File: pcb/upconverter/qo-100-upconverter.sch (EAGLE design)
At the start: 172 parts, among them CON1 3P-SH-SIDE, CON2 2EDG-2P-5MM, U1 EFM32TG11B120F128GM32, U10 MIC23155, U11 LT8636, U12 MCP3421-A0, U13 MCP6C02-020, U14 ADP7142AUJZ-3.3, U15 ADP7142AUJZ-3.3, U16 ADP3334, U17 ADM7171ACPZ-5.0, U2 DSB321SDA, U3 ADF4351, U4 F1951NBGI, U5 MAX2671, U6 2450BP15E0100, U7 F1478NLGA, U8 F1951NBGI, U9 ADL5606

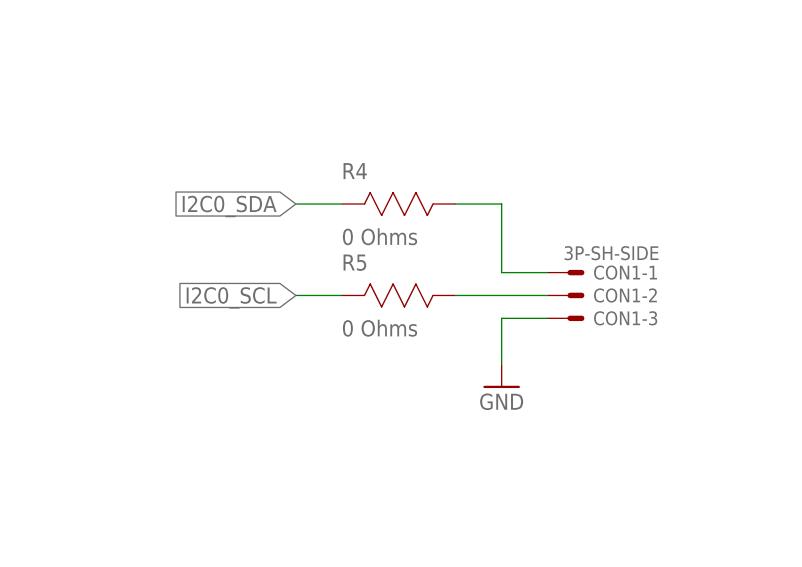
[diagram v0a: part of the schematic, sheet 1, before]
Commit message: Upconverter assembly BOM changes
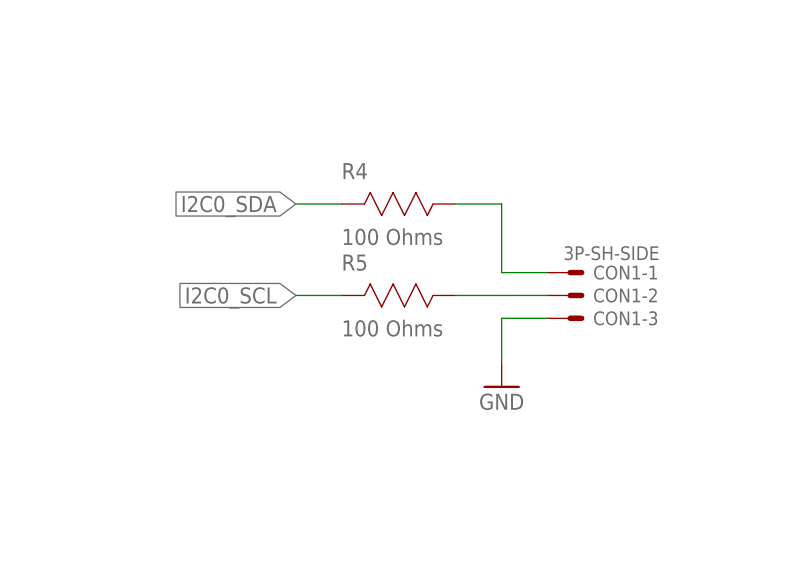
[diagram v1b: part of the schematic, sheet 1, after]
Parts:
- C25: value 100nF -> 150pF
- C27: value 100nF -> 150pF + 18 nH
- R4, R5: value 0 Ohms -> 100 Ohms
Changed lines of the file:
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@@
 <part name="U5" library="Maxim Integrated" deviceset="MAX2671" device=""/>
 <part name="RFCON1" library="RF Connector" deviceset="RFCON" device="-SMA-EDGE"/>
-<part name="C25" library="Capacitor" deviceset="CAPACITOR" device="-0603" value="100nF"/>
+<part name="C25" library="Capacitor" deviceset="CAPACITOR" device="-0603" value="150pF"/>
 <part name="GND2" library="Supply Symbol" deviceset="GND" device=""/>
 <part name="GND3" library="Supply Symbol" deviceset="GND" device=""/>
@@
 <part name="GND73" library="Supply Symbol" deviceset="GND" device=""/>
 <part name="U4" library="Renesas" deviceset="F1951*" device="" technology="NBGI"/>
-<part name="C27" library="Capacitor" deviceset="CAPACITOR" device="-0603" value="100nF"/>
+<part name="C27" library="Capacitor" deviceset="CAPACITOR" device="-0603" value="150pF + 18 nH"/>
 <part name="R14" library="Resistor" deviceset="RESISTOR" device="-0603" value="61.9 Ohms"/>
 <part name="R12" library="Resistor" deviceset="RESISTOR" device="-0603" value="105 Ohms"/>
@@
 <part name="CON1" library="JST" deviceset="3P" device="-SH-SIDE" value="3P-SH-SIDE"/>
 <part name="GND43" library="Supply Symbol" deviceset="GND" device=""/>
-<part name="R4" library="Resistor" deviceset="RESISTOR" device="-0603" value="0 Ohms"/>
-<part name="R5" library="Resistor" deviceset="RESISTOR" device="-0603" value="0 Ohms"/>
+<part name="R4" library="Resistor" deviceset="RESISTOR" device="-0603" value="100 Ohms"/>
+<part name="R5" library="Resistor" deviceset="RESISTOR" device="-0603" value="100 Ohms"/>
 <part name="U13" library="Microchip" deviceset="MCP6C02" device="" technology="-020"/>
 <part name="R36" library="Resistor" deviceset="RESISTOR" device="-1206" value="0.03 Ohms">

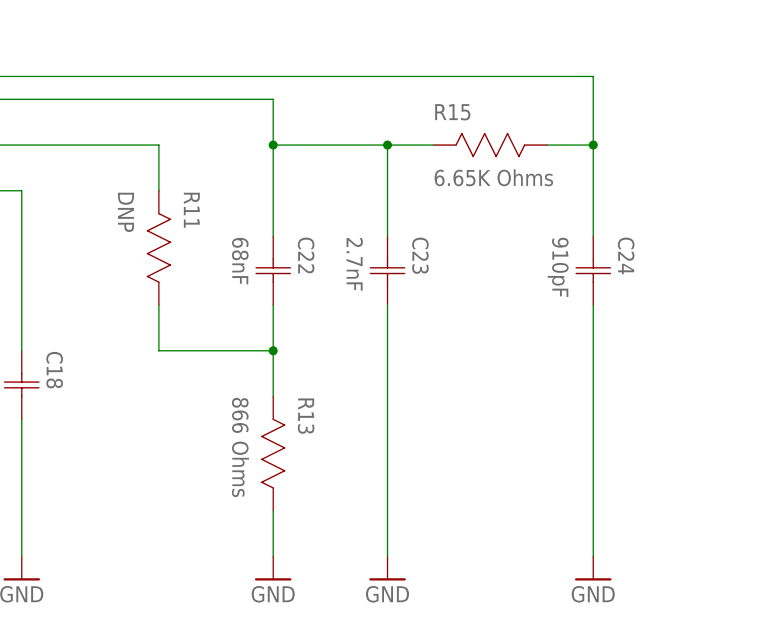
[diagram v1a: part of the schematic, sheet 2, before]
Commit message: Tweaking upconverter performance
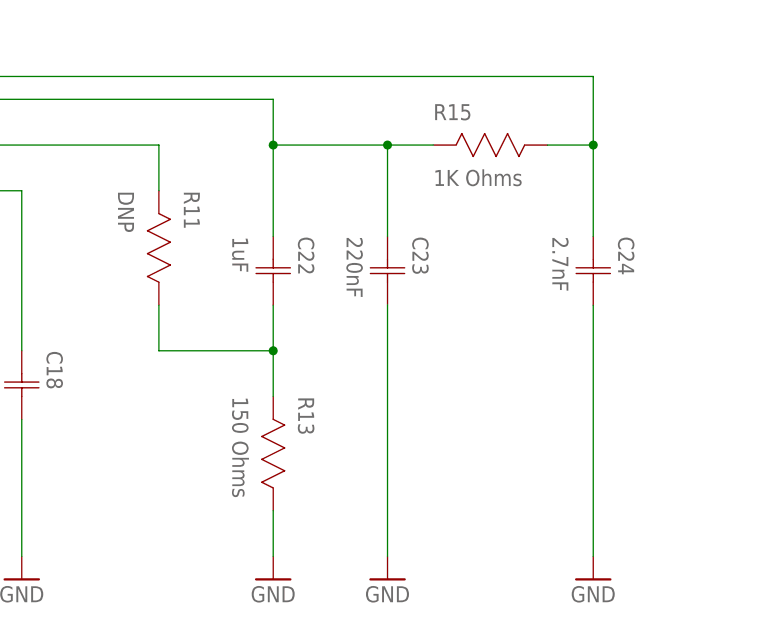
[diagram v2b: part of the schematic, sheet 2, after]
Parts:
- C22: value 68nF -> 1uF
- C23: value 2.7nF -> 220nF
- C24: value 910pF -> 2.7nF
- R13: value 866 Ohms -> 150 Ohms
- R15: value 6.65K Ohms -> 1K Ohms
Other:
- note added: "2kHz Loop Bandwidth at 2 mA"
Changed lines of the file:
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@@
 <part name="C10" library="Capacitor" deviceset="CAPACITOR" device="-0603" value="100nF"/>
 <part name="GND607" library="Supply Symbol" deviceset="GND" device=""/>
-<part name="C23" library="Capacitor" deviceset="CAPACITOR" device="-0603" value="2.7nF"/>
-<part name="C22" library="Capacitor" deviceset="CAPACITOR" device="-0603" value="68nF"/>
-<part name="R13" library="Resistor" deviceset="RESISTOR" device="-0603" value="866 Ohms"/>
-<part name="C24" library="Capacitor" deviceset="CAPACITOR" device="-0603" value="910pF"/>
-<part name="R15" library="Resistor" deviceset="RESISTOR" device="-0603" value="6.65K Ohms"/>
+<part name="C23" library="Capacitor" deviceset="CAPACITOR" device="-0603" value="220nF"/>
+<part name="C22" library="Capacitor" deviceset="CAPACITOR" device="-0603" value="1uF"/>
+<part name="R13" library="Resistor" deviceset="RESISTOR" device="-0603" value="150 Ohms"/>
+<part name="C24" library="Capacitor" deviceset="CAPACITOR" device="-0603" value="2.7nF"/>
+<part name="R15" library="Resistor" deviceset="RESISTOR" device="-0603" value="1K Ohms"/>
 <part name="GND618" library="Supply Symbol" deviceset="GND" device=""/>
 <part name="GND620" library="Supply Symbol" deviceset="GND" device=""/>
@@
 <plain>
 <text x="441.96" y="248.92" size="1.778" layer="98" align="center">-9 dB Pi Attenuator</text>
+<text x="444.5" y="170.18" size="1.778" layer="98" align="center">2kHz Loop Bandwidth at 2 mA</text>
 </plain>
 <instances>

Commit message: Upconverter v3 sent to production
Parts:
- added C100, C101, C99: 10uF, Capacitor:CAPACITOR-0603
- added C102, C103: 1nF, Capacitor:CAPACITOR-0603
- added C104: 10uF, Capacitor:CAPACITOR-1206
- added C87, C91, C92: 100nF, Capacitor:CAPACITOR-0603
- added C88: 10pF, Capacitor:CAPACITOR-0603
- added C89, C94, C95, C96, C97, C98: 1uF, Capacitor:CAPACITOR-0603
- added C90: 100uF, Capacitor:CAPACITOR-1206
- added C93: 22uF, Capacitor:CAPACITOR-1206
- added L12, L13: 3.3nH, Inductor:INDUCTOR-0603
- added L14: 1.8nH, Inductor:INDUCTOR-0603
- added L15: 1.5nH, Inductor:INDUCTOR-0603
- added L16: 470nH, Inductor:INDUCTOR-0603
- added L17: 2.2nH, Inductor:INDUCTOR-0603
- added L18: 62nH, Inductor:INDUCTOR-0603
- added L19: 0 Ohms, Inductor:INDUCTOR-0603
- added L20: 4.7uH, Inductor:INDUCTOR-6X6MM
- added R44: 75K Ohms, Resistor:RESISTOR-0603
- added R45: 41.2K Ohms, Resistor:RESISTOR-0603
- added R46: 1M Ohms, Resistor:RESISTOR-0603
- added R47: 221K Ohms, Resistor:RESISTOR-0603
- added R48, R49: 10K Ohms, Resistor:RESISTOR-0603
- added R50: 0.03 Ohms, Resistor:RESISTOR-1206
- added R51, R52: 100K Ohms, Resistor:RESISTOR-0603
- added R53: 1K Ohms, Resistor:RESISTOR-0603
- added RFCON5, RFCON6, RFCON7: RFCON-U.FL, RF Connector:RFCON-U.FL
- added RFCON8: RFCON-SMA-EDGE, RF Connector:RFCON-SMA-EDGE
- added SHIELD1: SHIELD-TE-2118728, Shield:SHIELD-TE-2118728
- added TP1, TP2, TP3, TP4, TP5, TP6: TESTPOINT-1.27MM, PADs:TESTPOINT-1.27MM
- added U18: MCP3421-A0, Microchip:MCP3421-A0
- added U19: MCP6C02-020, Microchip:MCP6C02-020
- added U20, U21, U22: ADP7142AUJZ-3.3, Analog Devices:ADP7142AUJZ-3.3
- added U23, U24: ADM7171ACPZ-5.0, Analog Devices:ADM7171ACPZ-5.0
- C10: value 100nF -> 10pF
- C25: value 150pF -> 1uF
- C26: value 100nF -> 1.2pF
- C27: value 150pF + 18 nH -> 100nF
- C28, C4: value 1uF -> 100nF
- C29: value 100nF -> 150pF
- C30: value 100pF -> 47pF
- C31: value 47pF -> 1.8pF
- C32: value 47pF -> 1.5pF
- C33: value 220pF -> 1.5pF
- C34: value 100uF -> 150pF; device Capacitor:CAPACITOR-1206 -> Capacitor:CAPACITOR-0603
- C35: value 1uF -> 220pF
- C36: value 1nF -> 100uF; device Capacitor:CAPACITOR-0603 -> Capacitor:CAPACITOR-1206
- C37: value 0.5pF -> 1uF
- C38, C55, C7: value 15pF -> 100nF
- C39: value 10pF -> 1uF
- C40: value 1uF -> 33pF
- C41: value 1nF -> 100nF
- C42: value 15pF -> 0.8pF
- C43, C9: value 10pF -> 100nF
- C44: value 1.2pF -> 10pF
- C45: value 100nF -> 47pF
- C46: value 15pF -> 1uF
- C47: value 10uF -> 15pF
- C48: value 10nF -> 100nF
- C49: value 100uF -> 33pF; device Capacitor:CAPACITOR-1206 -> Capacitor:CAPACITOR-0603
- C5: value 100nF -> 1uF
- C50: value 100pF -> 15pF
- C51: value 2pF -> 15pF
- C52: value 1uF -> 22pF
- C53: value 10nF -> 0.7pF
- C54: value 100pF -> 4.7uF
- C56: value 3.3pF -> 15pF
- C57: value 15pF -> 10nF
- C58: value 4.7uF -> 1uF; VOLTAGE 35V -> (none)
- C59: value 100nF -> 10uF
- C60: value 470pF -> 10nF
- C61: value 470pF -> 15pF
- C62: value 4.7uF -> 10nF
- C63: value 1uF -> 100uF; device Capacitor:CAPACITOR-0603 -> Capacitor:CAPACITOR-1206; VOLTAGE 50V -> (none)
- C64: value 470pF -> 100pF
- C65: value 1uF -> 2pF; VOLTAGE 50V -> (none)
- C68: value 100nF -> 100pF
- C69: value 100nF -> 15pF
- C70: value 10pF -> 3.3pF
- C71: value 1uF -> 15pF
- C73: value 100uF -> 15pF; device Capacitor:CAPACITOR-1206 -> Capacitor:CAPACITOR-0603
- C74: value 100uF -> 4.7uF; device Capacitor:CAPACITOR-1206 -> Capacitor:CAPACITOR-0603; VOLTAGE (none) -> 35V
- C76: value 100nF -> 470pF
- C77: value 22uF -> 470pF; device Capacitor:CAPACITOR-1206 -> Capacitor:CAPACITOR-0603
- C78: value 1uF -> 4.7uF
- C79, C80: VOLTAGE (none) -> 50V
- C82: value 10uF -> 10nF
- C83: value 10uF -> 100nF
- C84: value 1nF -> 10uF
- C85: value 470pF -> 10uF
- C86: value 10uF -> 100nF; device Capacitor:CAPACITOR-1206 -> Capacitor:CAPACITOR-0603; VOLTAGE 50V -> (none)
- L1: value 3.3nH -> 1uH
- L10: value 2.2uH -> 3.9nH; device Inductor:INDUCTOR-2.5X2X1.2MM -> Inductor:INDUCTOR-0603; CURRENT 2.2A -> (none); OCLCSC C375952 -> (none)
- L11: value 4.7uH -> 5.6nH; device Inductor:INDUCTOR-6X6MM -> Inductor:INDUCTOR-0603; CURRENT 3A -> (none); OCLCSC C326336 -> (none)
- L2: value 10nH -> 3.3nH
- L3: value 3.3nH -> 10nH
- L5: value 1.8nH -> 4.7nH
- L6: value 3.9nH -> 12nH
- L7: value 3nH -> 3.3nH
- L8: value 62nH -> 3.9nH
- L9: value 62nH -> 18nH
- R10: value 5.1K Ohms -> 100K Ohms
- R11: value DNP -> 330 Ohms
- R12: value 105 Ohms -> 0 Ohms
- R13: value 150 Ohms -> 10K Ohms
- R14: value 61.9 Ohms -> 5.1K Ohms
- R15, R23: value 1K Ohms -> DNP
- R17: value 1K Ohms -> 150 Ohms
- R18: value 100 Ohms -> 61.9 Ohms
- R19: value 100K Ohms -> 1K Ohms
- R20: value 0 Ohms -> 105 Ohms; device Resistor:RESISTOR-SEL-0603 -> Resistor:RESISTOR-0603
- R22, R24: value 510 Ohms -> 0 Ohms
- R25: value 100K Ohms -> DNP
- R26, R35: value 10K Ohms -> DNP
- R27: value 100K Ohms -> 0 Ohms
- R28: value 75K Ohms -> 1K Ohms
- R29: value 41.2K Ohms -> 0 Ohms
- R30: value 309K Ohms -> DNP
- R31: value 71.5K Ohms -> 1.5K Ohms
- R32: value 1M Ohms -> 0 Ohms
- R33: value 221K Ohms -> 510 Ohms
- R34: value 10K Ohms -> 0 Ohms
- R36: value 0.03 Ohms -> 1K Ohms; device Resistor:RESISTOR-1206 -> Resistor:RESISTOR-0603; TOLERANCE 1% -> (none)
- R37: value 100K Ohms -> 2K Ohms
- R38, R7: value 100K Ohms -> 100 Ohms
- R39: value 210K Ohms -> 49.9 Ohms
- R4, R5: value 100 Ohms -> 1K Ohms
- R40: value 64.9K Ohms -> 510 Ohms
- R41: value 510 Ohms -> 100K Ohms
- R43: value 0 Ohms -> 100K Ohms
- R6: value 330 Ohms -> 100 Ohms
- R8: value 100K Ohms -> 330 Ohms
- R9: value 330 Ohms -> 100K Ohms
- RFCON1, RFCON3: value RFCON-SMA-EDGE -> RFCON-U.FL; device RF Connector:RFCON-SMA-EDGE -> RF Connector:RFCON-U.FL
- RFCON2: value RFCON-U.FL -> RFCON-SMA-EDGE; device RF Connector:RFCON-U.FL -> RF Connector:RFCON-SMA-EDGE
- U10: value MIC23155 -> LTC5597; device Microchip:MIC23155 -> Analog Devices:LTC5597
- U11: value LT8636 -> 2450BP15E0100; device Analog Devices:LT8636 -> Generic Filter:2450BP15E0100
- U12: value MCP3421-A0 -> MCP6V31; device Microchip:MCP3421-A0 -> Microchip:MCP6V31
- U13: value MCP6C02-020 -> DC2337J5010AHF; device Microchip:MCP6C02-020 -> Anaren:DC2337J5010AHF; OCLCSC (none) -> C509396
- U14: value ADP7142AUJZ-3.3 -> ADL5606; device Analog Devices:ADP7142AUJZ-3.3 -> Analog Devices:ADL5606
- U15: value ADP7142AUJZ-3.3 -> F1958NBGK; device Analog Devices:ADP7142AUJZ-3.3 -> Renesas:F1958NBGK
- U16: value ADP3334 -> MCP1700-330; device Analog Devices:ADP3334 -> Microchip:MCP1700-330
- U17: value ADM7171ACPZ-5.0 -> LT8636; device Analog Devices:ADM7171ACPZ-5.0 -> Analog Devices:LT8636
- U4: value F1951NBGI -> F1958NBGK; device Renesas:F1951NBGI -> Renesas:F1958NBGK
- U7: value F1478NLGA -> F1958NBGK; device Renesas:F1478NLGA -> Renesas:F1958NBGK
- U8: value F1951NBGI -> ADL5601; device Renesas:F1951NBGI -> Analog Devices:ADL5601
- U9: value ADL5606 -> F1490NLGA; device Analog Devices:ADL5606 -> Renesas:F1490NLGA
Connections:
- removed net !IF_ATT_CS: U1.PC13, U4.!CS
- removed net !PA_STG1_BIAS_EN: R38.1, U1.PA2, U16.SD
- removed net !RF_ATT_CS: U1.PA1, U8.!CS
- removed net 3V3_ATT_MIXER_CLEAN: C26.C1, C28.C1, C29.C1, C31.C1, C32.C1, C45.C1, C7.C1, C82.C1, L5.2, U14.SENSE/ADJ, U14.VOUT, U4.VDD, U5.VCC, U8.VDD
- removed net 3V3_FB: R30.1, R31.2, U10.FB
- removed net 3V3_SOFTSTART: C64.C1, U10.SS
- removed net 3V3_SW: L10.1, U10.SW
- removed net 5V0_PA_STG1_CLEAN: C34.C1, C35.C1, C36.C1, C38.C1, C40.C1, C41.C1, C42.C1, C85.C1, L7.2, L8.2, R22.2, R39.2, U16.OUT, U7.BIAS1
- removed net 5V0_PA_STG2_CLEAN: C47.C1, C48.C1, C49.C1, C50.C1, C52.C1, C53.C1, C54.C1, C55.C1, L9.2, R24.2, U17.SENSE, U17.VOUT, U9.VBIAS, U9.VCC
- removed net N$14: C43.C1, L8.1, U7.RFOUT
- removed net N$18: C57.C2, RFCON3.SIGNAL
- removed net N$26: C25.C2, U4.RF2
- removed net N$27: C27.C2, U5.IFIN
- removed net N$31: C33.C2, R20.2
- removed net N$9: C46.C1, U8.RF1
- removed net PA_STG2_BIAS_EN: R37.2, U1.PC0, U17.EN
- removed net RF_ACC_FILT: C37.C1, C39.C1, U6.RFOUT
- removed net RF_ACC_PRE: C43.C2, C44.C1, U8.RF2
- new net 3V3_IF_ATT_MIXER_CLEAN: C25.C1, C27.C1, C28.C1, C30.C1, C99.C1, L14.2, U20.SENSE/ADJ, U20.VOUT, U4.VDD, U4.VMODE, U5.VCC
- new net 3V3_RF_ATT_PDET_CLEAN: C100.C1, C41.C1, C54.C1, C55.C1, C72.C1, U10.EN, U10.VCC, U12.PWR.V+, U15.VDD, U15.VMODE, U21.SENSE/ADJ, U21.VOUT, U7.VDD, U7.VMODE
- new net 5V0_PA_STG1_2_CLEAN: C36.C1, C37.C1, C38.C1, C39.C1, C40.C1, C43.C1, C45.C1, C46.C1, C47.C1, C48.C1, C49.C1, L15.2, L16.2, L17.2, R28.2, R29.2, R31.2, R33.2, U23.SENSE, U23.VOUT
- new net 5V0_PA_STG3_CLEAN: C59.C1, C60.C1, C63.C1, C64.C1, C66.C1, C67.C1, C68.C1, C69.C1, L18.2, R40.2, U14.VBIAS, U14.VCC, U24.SENSE, U24.VOUT
- new net IF_ATT_ACC: L9.1, R24.1
- new net IF_ATT_ACC_PROBE: C34.C2, R23.1, R24.2
- new net IF_ATT_DCC: C34.C1, U4.RF1
- new net IF_ATT_LE: U1.PD6, U4.LE
- new net IF_IN_ACC: C29.C2, U4.RF2
- new net MIXER_IN_DCC: L9.2, U5.IFIN
- new net MIXER_OUT_ACC_PROBE: C35.C2, R26.1, R27.2
- new net MIXER_OUT_DCC: L13.1, U5.RFOUT
- new net N$24: R23.2, RFCON3.SIGNAL
- new net N$33: C31.C2, C32.C1, L10.2, L11.1, L8.2
- new net N$34: C32.C2, C33.C1, L11.2, L12.2
- new net N$35: R30.2, RFCON6.SIGNAL
- new net N$39: L19.2, U15.RF2
- new net N$42: R39.2, U13.ISOLATED
- new net N$43: C56.C1, U10.RFIN
- new net N$44: C57.C2, U10.FLTR
- new net N$45: R22.2, U5.LO
- new net N$47: R25.1, RFCON4.SIGNAL
- new net N$48: R35.2, RFCON7.SIGNAL
- new net PA_STG1_2_BIAS_EN: R51.2, U1.PB7, U23.EN
- new net PA_STG3_BIAS_EN: R52.2, U1.PB8, U24.EN
- new net RF_ATT1_LE: U1.PA1, U7.LE
- new net RF_ATT2_LE: U1.PA2, U15.LE
- new net RF_FINAL_ACC: C71.C2, RFCON8.SIGNAL
- new net RF_FINAL_DCC: C70.C1, C71.C1, L18.1, U14.RFOUT
- new net RF_LOL_FLT_ACC: C33.C2, U8.RFIN
- new net RF_PRE1_ACC: C51.C2, U7.RF2
- new net RF_PRE1_ATT_ACC: R32.1, U6.RFIN
- new net RF_PRE1_ATT_ACC_PROBE: C50.C2, R30.1, R32.2
- new net RF_PRE1_ATT_DCC: C50.C1, U7.RF1
- new net RF_PRE1_ATT_FLT_ACC: C42.C1, C44.C1, U6.RFOUT
- new net RF_PRE1_DCC: C51.C1, L16.1, U8.RFOUT
- new net RF_PRE2_ACC: C52.C2, C53.C1, L19.1
- new net RF_PRE2_ATT_ACC: C73.C2, U11.RFIN
- new net RF_PRE2_ATT_DCC: C73.C1, U15.RF1
- new net RF_PRE2_ATT_FLT_ACC: U11.RFOUT, U13.IN
- new net RF_PRE2_ATT_FLT_CPL_ACC: C56.C2, R35.1, U13.COUPLED
- new net RF_PRE2_ATT_FLT_THRU_ACC: C61.C1, U13.OUT
- new net RF_PRE2_DCC: C52.C1, L17.1, U9.RFOUT
- new net VPDET_AMP: R37.1, R38.2, U12.1.OUT
- new net VPDET_FLT: C58.C1, R34.1, U12.1.+IN
- new net VPDET_RAW: C57.C1, R34.2, U10.OUT
- new net VPDET_SENSE: C62.C1, R38.1, U1.PA0
- net !MIXER_SHDN: now also R21.2, U1.PD7, U5.!SHDN; no longer R18.2, U1.PC14
- net !PLL_MUTE: now also R10.2; no longer R8.2
- net 3V3: now also C4.C1, C83.C1, C84.C1, C85.C1, C86.C1, R4.2, R5.2, U16.VOUT, U18.VDD; no longer C11.C1, C68.C1, C72.C1, C73.C1, L10.2, R17.2, R23.2, R30.2, R38.2, U10.SNS, U12.VDD, U3.DVDD
- net 3V3_PLL_CLEAN: now also C101.C1, C7.C1, C9.C1, L1.2, L2.1, L3.2, U22.SENSE/ADJ, U22.VOUT; no longer C10.C1, C5.C1, C83.C1, L1.1, L2.2, U15.SENSE/ADJ, U15.VOUT
- net 5V0: now also C75.C1, C78.C1, C88.C1, C89.C1, C90.C1, C92.C1, L20.2, R43.2, R46.2, R50.2, R53.2, U16.VIN, U17.BIAS, U19.VDD, U19.VIP; no longer C59.C1, C62.C1, C70.C1, C71.C1, C74.C1, C76.C1, L11.2, R27.2, R32.2, R36.2, R41.2, U10.EN, U10.VIN@0, U10.VIN@1, U11.BIAS, U13.VDD, U13.VIP
- net 5V0_BST: now also C87.C2, U17.BST; no longer C69.C2, U11.BST
- net 5V0_FB: now also C88.C2, R46.1, R47.2, U17.FB; no longer C70.C2, R32.1, R33.2, U11.FB
- net 5V0_INTVCC: now also C81.C1, U17.INTVCC, U17.SYNC/MODE; no longer C66.C1, U11.INTVCC, U11.SYNC/MODE
- net 5V0_ISENSE: now also C93.C1, C94.C1, C95.C1, C96.C1, C97.C1, C98.C1, R50.1, U19.VIM, U20.EN, U20.VIN, U21.EN, U21.VIN, U22.EN, U22.VIN, U23.VIN, U24.VIN; no longer C77.C1, C78.C1, C79.C1, C80.C1, C81.C1, R36.1, U13.VIM, U14.EN, U14.VIN, U15.EN, U15.VIN, U16.IN, U17.VIN
- net 5V0_ISENSE_VN: now also C91.C2, R49.1, U18.VIN-; no longer C75.C2, R35.1, U12.VIN-
- net 5V0_ISENSE_VP: now also C91.C1, R48.1, U18.VIN+; no longer C75.C1, R34.1, U12.VIN+
- net 5V0_RT: now also R45.2, U17.RT; no longer R29.2, U11.RT
- net 5V0_SS: now also C82.C1, U17.TR/SS; no longer C67.C1, U11.TR/SS
- net 5V0_SW: now also C87.C1, L20.1, U17.SW; no longer C69.C1, L11.1, U11.SW
- net 5V0_VSENSE: now also C77.C1, R43.1, R44.2; no longer C61.C1, R27.1, R28.2
- net GND: now also C100.C2, C101.C2, C102.C2, C103.C2, C104.C2, C25.C2, C27.C2, C39.C2, C43.C2, C46.C2, C69.C2, C70.C2, C75.C2, C85.C2, C89.C2, C90.C2, C92.C2, C93.C2, C94.C2, C95.C2, C96.C2, C97.C2, C98.C2, C99.C2, L10.1, L12.1, L5.1, L7.1, R14.1, R17.1, R20.1, R36.1, R39.1, R44.1, R45.1, R47.1, R49.2, R51.1, R52.1, R9.1, RFCON5.GND, RFCON6.GND, RFCON7.GND, RFCON8.GND, SHIELD1.GND, TP1.TP, TP2.TP, TP3.TP, TP4.TP, TP5.TP, TP6.TP, U10.GND@0, U10.GND@1, U10.GND@2, U10.GND@3, U12.PWR.V-, U13.GND, U14.DISABLE, U15.D0, U15.D1, U15.D2, U15.D3, U15.D4, U15.D5, U15.D6, U18.VSS, U19.VREF, U19.VSS, U20.GND, U21.GND, U22.GND, U23.GND, U24.GND, U4.D0, U4.D1, U4.D2, U4.D3, U4.D4, U4.D5, U4.D6, U7.D0, U7.D1, U7.D2, U7.D3, U7.D4, U7.D5, U7.D6, U8.GND@0, U8.GND@1; no longer C26.C2, C29.C2, C31.C2, C32.C2, C34.C2, C35.C2, C44.C2, C50.C2, C51.C2, C52.C2, C56.C2, C61.C2, C71.C2, C73.C2, L6.1, R12.1, R19.1, R26.1, R28.1, R29.1, R31.1, R33.1, R35.2, R37.1, R40.1, R7.1, R8.1, U10.AGND, U10.PGND@0, U10.PGND@1, U12.VSS, U13.VREF, U13.VSS, U8.GND, U9.DISABLE
- net I2C0_SCL: now also R4.1, R7.2, U1.PC1; no longer R17.1, R5.2, U1.PD7
- net I2C0_SDA: now also R5.1, R6.2, U1.PC0; no longer R23.1, R4.2, U1.PD6
- net I2C1_SCL: now also U18.SCL; no longer U12.SCL
- net I2C1_SDA: now also U18.SDA; no longer U12.SDA
- net IF_IN_DCC: now also C29.C1, RFCON2.SIGNAL; no longer C25.C1, RFCON1.SIGNAL
- net LED: now also R8.2, U1.PB11; no longer R6.2, U1.PB7
- net MIXER_LO: now also R18.1, R20.2, R22.1, R25.2; no longer R14.1, R16.2, U5.LO
- net N$1: now also L4.2; no longer L3.1
- net N$10: now also R48.2, U19.VOUT; no longer R34.2, U13.VOUT
- net N$11: now also R7.1; no longer R5.1
- net N$12: now also L15.1, U9.VDD; no longer L7.1, U7.VCC
- net N$13: now also R11.1; no longer R9.1
- net N$149: now also R53.1; no longer R41.1
- net N$15: now also R28.1, U9.BIAS1; no longer R21.2, U7.RSET
- net N$16: now also R31.1, U9.BIAS2; no longer L6.2, U7.BIAS2
- net N$17: now also R6.1; no longer R4.1
- net N$2: now also C103.C1, U24.SS; no longer C84.C1, U17.SS
- net N$20: now also C102.C1, U23.SS; no longer C85.C2, R39.1, R40.2, U16.FB
- net N$21: now also R12.2, RFCON1.SIGNAL; no longer R43.2, RFCON4.SIGNAL
- net N$22: now also C5.C1; no longer C4.C1
- net N$23: now also R33.1; no longer R22.1
- net N$25: now also R8.1; no longer R6.1
- net N$28: now also R26.2, RFCON5.SIGNAL; no longer C27.C1, U4.RF1
- net N$29: now also R16.2, R18.2; no longer R12.2, R14.2
- net N$3: now also R40.1; no longer R24.1
- net N$30: now also C44.C2, U9.RFIN; no longer C39.C2, U7.RFIN
- net N$32: now also C26.C2, C31.C1, L6.2, L7.2, L8.1; no longer R20.COM, RFCON2.SIGNAL
- net N$4: now also R29.1, U9.GAIN_SEL; no longer C30.C1, R18.1, R19.2, U5.!SHDN
- net N$5: now also C61.C2, C65.C1, U14.RFIN; no longer C46.C2, C51.C1, U9.RFIN
- net N$6: now also C35.C1, L13.2, L14.1; no longer C33.C1, L4.2, L5.1
- net N$67: now also L3.1, L4.1; no longer L2.1, L3.2
- net N$69: now also L2.2; no longer L1.2
- net N$7: now also R36.2, R37.2, U12.1.-IN; no longer L4.1, U5.RFOUT
- net N$8: now also C11.C1, L1.1, U3.DVDD; no longer C56.C1, C57.C1, L9.1, U9.RFOUT
- net N$84: now also R15.1, R17.2; no longer R11.1, R13.2
- net N$88: now also R14.2; no longer R10.2
- net PLL_CP_VOUT: now also R19.2; no longer R15.2
- net PLL_EN: now also R9.2, U1.PC14; no longer R7.2, U1.PC15
- net PLL_FASTLOCK_SW: now also R15.2; no longer R11.2
- net PLL_LE: now also U1.PC15; no longer U1.PA0
- net PLL_LOCK: now also R11.2; no longer R9.2
- net PLL_REF_DCC: now also C10.C1, R12.1, R13.2; no longer C9.C1, R42.2, R43.1
- net PLL_VTUNE: now also R19.1; no longer R15.1
- net RF_ACC: now also C26.C1, L5.2, L6.1, R27.1; no longer R20.1, U6.RFIN
- net SPI_MOSI: now also U15.DATA, U4.DATA, U7.DATA; no longer U4.SDI, U8.SDI
- net SPI_SCK: now also U15.CLK, U7.CLK; no longer U8.CLK
- net VIN: now also C104.C1, C74.C1, C79.C1, C80.C1, R41.2, U17.EN/UV, U17.VIN; no longer C58.C1, C63.C1, C65.C1, C86.C1, R25.2, U11.EN/UV, U11.VIN
- net VIN_VSENSE: now also C76.C1, R41.1, R42.2; no longer C60.C1, R25.1, R26.2
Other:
- note added: "+13.8 dB"
- note added: "+39.5 dB"
- note added: "-0.1 dB at 2.4 GHz -55 dB 1.875 GHz"
- note removed: "+30 dB"

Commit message: Upconverter v3 software Upconverter assembly and tuning schematic changes Upconverter test documentation added
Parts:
- C22: value 1uF -> 20nF
- C23: value 220nF -> 1nF
- C24: value 2.7nF -> 470pF
- C29, C34: value 150pF -> 100pF
- C31: value 1.8pF -> DNP
- C32: value 1.5pF -> DNP
- C33: value 1.5pF -> 12pF
- L10: value 3.9nH -> 1.8pF
- L11: value 5.6nH -> 0 Ohms
- L12: value 3.3nH -> 2.2pF
- L5: value 4.7nH -> 5.1nH
- L6: value 12nH -> 5.1nH
- L8: value 3.9nH -> 0 Ohms
- R17: value 150 Ohms -> 330 Ohms
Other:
- note added: "100kHz Loop Bandwidth at 2.5 mA"
- note removed: "-0.1 dB at 2.4 GHz -55 dB 1.875 GHz"
- note removed: "2kHz Loop Bandwidth at 2 mA"
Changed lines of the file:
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@@
 <part name="C9" library="Capacitor" deviceset="CAPACITOR" device="-0603" value="100nF"/>
 <part name="GND607" library="Supply Symbol" deviceset="GND" device=""/>
-<part name="C23" library="Capacitor" deviceset="CAPACITOR" device="-0603" value="220nF"/>
-<part name="C22" library="Capacitor" deviceset="CAPACITOR" device="-0603" value="1uF"/>
-<part name="R17" library="Resistor" deviceset="RESISTOR" device="-0603" value="150 Ohms"/>
-<part name="C24" library="Capacitor" deviceset="CAPACITOR" device="-0603" value="2.7nF"/>
+<part name="C23" library="Capacitor" deviceset="CAPACITOR" device="-0603" value="1nF"/>
+<part name="C22" library="Capacitor" deviceset="CAPACITOR" device="-0603" value="20nF"/>
+<part name="R17" library="Resistor" deviceset="RESISTOR" device="-0603" value="330 Ohms"/>
+<part name="C24" library="Capacitor" deviceset="CAPACITOR" device="-0603" value="470pF"/>
 <part name="R19" library="Resistor" deviceset="RESISTOR" device="-0603" value="1K Ohms"/>
 <part name="GND618" library="Supply Symbol" deviceset="GND" device=""/>
@@
 <part name="U5" library="Maxim Integrated" deviceset="MAX2671" device=""/>
 <part name="RFCON2" library="RF Connector" deviceset="RFCON" device="-SMA-EDGE"/>
-<part name="C29" library="Capacitor" deviceset="CAPACITOR" device="-0603" value="150pF"/>
+<part name="C29" library="Capacitor" deviceset="CAPACITOR" device="-0603" value="100pF"/>
 <part name="GND2" library="Supply Symbol" deviceset="GND" device=""/>
 <part name="GND3" library="Supply Symbol" deviceset="GND" device=""/>
@@
 <part name="C28" library="Capacitor" deviceset="CAPACITOR" device="-0603" value="100nF"/>
 <part name="GND73" library="Supply Symbol" deviceset="GND" device=""/>
-<part name="C34" library="Capacitor" deviceset="CAPACITOR" device="-0603" value="150pF"/>
+<part name="C34" library="Capacitor" deviceset="CAPACITOR" device="-0603" value="100pF"/>
 <part name="R18" library="Resistor" deviceset="RESISTOR" device="-0603" value="61.9 Ohms"/>
 <part name="R16" library="Resistor" deviceset="RESISTOR" device="-0603" value="105 Ohms"/>
@@
 <part name="R27" library="Resistor" deviceset="RESISTOR" device="-0603" value="0 Ohms"/>
 <part name="R26" library="Resistor" deviceset="RESISTOR" device="-0603" value="DNP"/>
-<part name="L5" library="Inductor" deviceset="INDUCTOR" device="-0603" value="4.7nH"/>
+<part name="L5" library="Inductor" deviceset="INDUCTOR" device="-0603" value="5.1nH"/>
 <part name="GND12" library="Supply Symbol" deviceset="GND" device=""/>
 <part name="L7" library="Inductor" deviceset="INDUCTOR" device="-0603" value="3.3nH"/>
 <part name="GND66" library="Supply Symbol" deviceset="GND" device=""/>
 <part name="C26" library="Capacitor" deviceset="CAPACITOR" device="-0603" value="1.2pF"/>
-<part name="C31" library="Capacitor" deviceset="CAPACITOR" device="-0603" value="1.8pF"/>
-<part name="C32" library="Capacitor" deviceset="CAPACITOR" device="-0603" value="1.5pF"/>
-<part name="C33" library="Capacitor" deviceset="CAPACITOR" device="-0603" value="1.5pF"/>
-<part name="L10" library="Inductor" deviceset="INDUCTOR" device="-0603" value="3.9nH"/>
+<part name="C31" library="Capacitor" deviceset="CAPACITOR" device="-0603" value="DNP"/>
+<part name="C32" library="Capacitor" deviceset="CAPACITOR" device="-0603" value="DNP"/>
+<part name="C33" library="Capacitor" deviceset="CAPACITOR" device="-0603" value="12pF"/>
+<part name="L10" library="Inductor" deviceset="INDUCTOR" device="-0603" value="1.8pF"/>
 <part name="GND77" library="Supply Symbol" deviceset="GND" device=""/>
-<part name="L12" library="Inductor" deviceset="INDUCTOR" device="-0603" value="3.3nH"/>
+<part name="L12" library="Inductor" deviceset="INDUCTOR" device="-0603" value="2.2pF"/>
 <part name="GND78" library="Supply Symbol" deviceset="GND" device=""/>
 <part name="U8" library="Analog Devices" deviceset="ADL5?" device="" technology="601"/>
@@
 <part name="R32" library="Resistor" deviceset="RESISTOR" device="-0603" value="0 Ohms"/>
 <part name="R30" library="Resistor" deviceset="RESISTOR" device="-0603" value="DNP"/>
-<part name="L6" library="Inductor" deviceset="INDUCTOR" device="-0603" value="12nH"/>
-<part name="L8" library="Inductor" deviceset="INDUCTOR" device="-0603" value="3.9nH"/>
-<part name="L11" library="Inductor" deviceset="INDUCTOR" device="-0603" value="5.6nH"/>
+<part name="L6" library="Inductor" deviceset="INDUCTOR" device="-0603" value="5.1nH"/>
+<part name="L8" library="Inductor" deviceset="INDUCTOR" device="-0603" value="0 Ohms"/>
+<part name="L11" library="Inductor" deviceset="INDUCTOR" device="-0603" value="0 Ohms"/>
 <part name="U13" library="Anaren" deviceset="DC2337J5010AHF" device="">
 <attribute name="OCLCSC" value="C509396"/>
@@
 <plain>
 <text x="441.96" y="248.92" size="1.778" layer="98" align="center">-9 dB Pi Attenuator</text>
-<text x="444.5" y="170.18" size="1.778" layer="98" align="center">2kHz Loop Bandwidth at 2 mA</text>
+<text x="441.96" y="170.18" size="1.778" layer="98" align="center">100kHz Loop Bandwidth at 2.5 mA</text>
 </plain>
 <instances>
@@
 <text x="297.18" y="205.74" size="1.778" layer="98" align="center">+9 dB</text>
 <text x="289.56" y="325.12" size="1.778" layer="98" align="center">-1.2 dB to -32.5 dB</text>
-<text x="256.54" y="91.44" size="1.778" layer="98" align="center">-0.1 dB at 2.4 GHz
--55 dB 1.875 GHz</text>
 </plain>
 <instances>
